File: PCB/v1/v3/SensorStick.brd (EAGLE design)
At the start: 76.2 x 44.5 mm, 74 parts, among them U1 TPD4F003DQDR, Y1 ECS-TXO-3225MV-400-TR

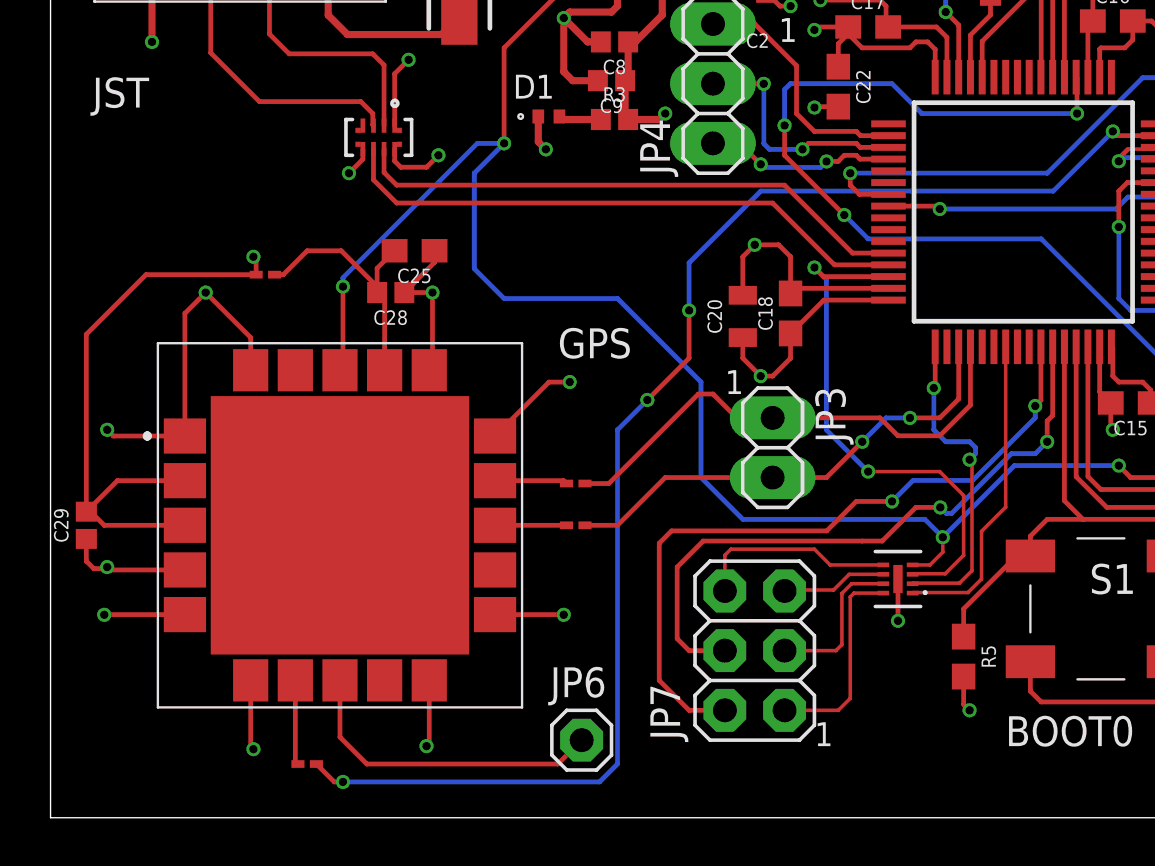
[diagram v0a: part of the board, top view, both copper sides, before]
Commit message: Jesus - Began to transition GPS to header pins
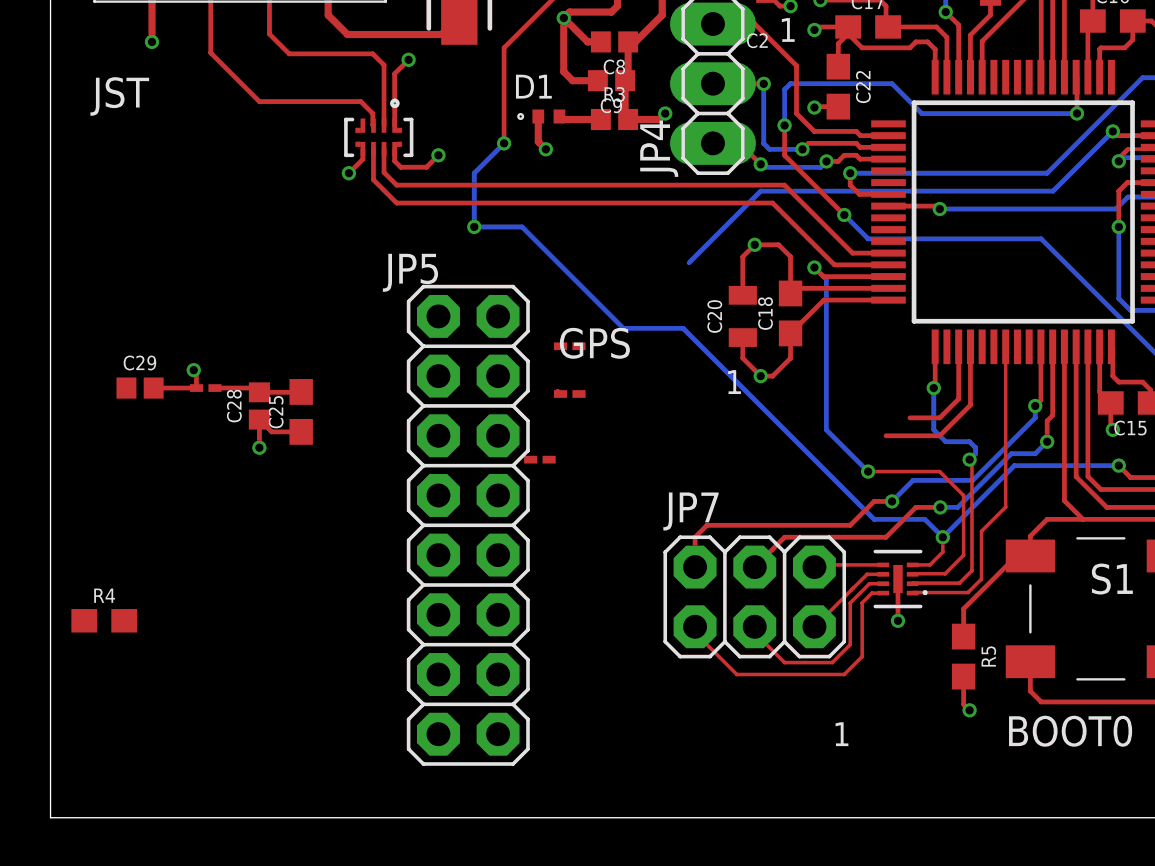
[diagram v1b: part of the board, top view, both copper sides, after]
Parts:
- removed GPS: SAM-M8Q-0-10, SAM-M8Q-0-10:SAMM8Q010
- removed JP3: (no value), pinhead:1X02
- removed JP6: (no value), pinhead:1X01
- added JP5: (no value), pinhead:2X08
- added R4: 0, SparkFun-Resistors:0603
- moved L4 16.3 mm to (20.8, 15.2)
- moved C25 8.39 mm to (10.7, 17.3), turned to 90 degrees
- moved L2 7.62 mm to (22.1, 20.1)
- moved C28 7.38 mm to (8.89, 17.5), turned to 90 degrees
- moved C29 6.27 mm to (3.81, 18.3), turned to 0 degrees
- moved L6 5.45 mm to (6.60, 18.3)
- moved L5 3.82 mm to (22.1, 18.0)
- moved JP7 2.29 mm to (30.0, 9.40), turned to 0 degrees
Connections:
- removed net N$2: GPS.7, L4.2
- removed net N$9: C25.2, C28.2, GPS.17, L6.1
- new net TIMEPULSE: JP5.6, L4.2
- new net VCC: JP5.1
- new net VCC_GPS: C25.2, C28.2, L6.1
- new net VCC_IO: JP5.7
- new net V_BACKUP: JP5.5
- net 3V3: now also R4.1, R4.2; no longer GPS.2, GPS.3
- net GND: now also JP5.10, JP5.11, JP5.12, JP5.13, JP5.14, JP5.15, JP5.16, JP5.9; no longer GPS.1, GPS.10, GPS.11, GPS.15, GPS.16, GPS.20, GPS.4, GPS.5, GPS.6
- net GPS_SAFEBOOT: now also JP5.8; no longer GPS.8, JP6.1
- net NRST: now also JP5.3; no longer GPS.18
- net RX: now also JP5.4; no longer GPS.14
- net TX: now also JP5.2; no longer GPS.13
- net USART3_RX: no longer JP3.1
- net USART3_TX: no longer JP3.2
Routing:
- net GND: track 180.0 -> 140.6 mm, vias 39 -> 31
- net GPIO_EXTI1: track 58.4 -> 22.4 mm, vias 4 -> 1
- net 3V3: track 146.6 -> 123.4 mm
- net NRST: track 115.0 -> 98.4 mm
- net USART3_TX: track 20.4 -> 4.63 mm, vias 2 -> 0
- net USART3_RX: track 21.7 -> 6.61 mm
- net GPS_SAFEBOOT: track 13.6 -> 0.00 mm
- net N$9: track 10.9 -> 0.00 mm
- net USART1_TX: track 30.5 -> 21.0 mm
- net USART1_RX: track 27.6 -> 18.8 mm
- net NRST_O: track 8.65 -> 2.97 mm
- net VCC_GPS: track 0.00 -> 4.31 mm
- net N$2: track 3.61 -> 0.00 mm
- net TX: track 3.04 -> 0.00 mm
- net SWO_O: track 8.80 -> 11.8 mm
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
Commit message: Jesus - Cleaning up GPS schematic
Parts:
- moved L4 1.27 mm to (21.8, 16.0)
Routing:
- net I2C3_SDA: track 37.3 -> 19.8 mm, vias 2 -> 1
- net I2C3_SCL: track 36.0 -> 20.8 mm, vias 2 -> 1
- net NRST: track 98.4 -> 94.5 mm, vias 4 -> 3
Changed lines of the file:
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@@
 <attribute name="NAME" x="23.9014" y="20.447" size="1.27" layer="27" ratio="6" rot="SR0"/>
 </element>
-<element name="L4" library="BLM03AG601SN1D" package="IND_BLM03_0201_MUR" value="BLM03AG601SN1D" x="20.828" y="15.24" smashed="yes" rot="R180">
-<attribute name="COPYRIGHT" value="Copyright (C) 2023 Ultra Librarian. All rights reserved." x="20.828" y="15.24" size="1.778" layer="27" rot="R180" display="off"/>
-<attribute name="DIGI-KEY_PART_NUMBER_1" value="490-5164-1-ND" x="20.828" y="15.24" size="1.778" layer="27" rot="R180" display="off"/>
-<attribute name="DIGI-KEY_PART_NUMBER_2" value="490-5164-2-ND" x="20.828" y="15.24" size="1.778" layer="27" rot="R180" display="off"/>
-<attribute name="DIGI-KEY_PART_NUMBER_3" value="490-5164-6-ND" x="20.828" y="15.24" size="1.778" layer="27" rot="R180" display="off"/>
-<attribute name="MANUFACTURER_PART_NUMBER" value="BLM03AG601SN1D" x="20.828" y="15.24" size="1.778" layer="27" rot="R180" display="off"/>
-<attribute name="MFR_NAME" value="Murata" x="20.828" y="15.24" size="1.778" layer="27" rot="R180" display="off"/>
-<attribute name="NAME" x="21.6154" y="13.843" size="1.27" layer="27" ratio="6" rot="SR0"/>
+<element name="L4" library="BLM03AG601SN1D" package="IND_BLM03_0201_MUR" value="BLM03AG601SN1D" x="21.844" y="16.002" smashed="yes" rot="R180">
+<attribute name="COPYRIGHT" value="Copyright (C) 2023 Ultra Librarian. All rights reserved." x="21.844" y="16.002" size="1.778" layer="27" rot="R180" display="off"/>
+<attribute name="DIGI-KEY_PART_NUMBER_1" value="490-5164-1-ND" x="21.844" y="16.002" size="1.778" layer="27" rot="R180" display="off"/>
+<attribute name="DIGI-KEY_PART_NUMBER_2" value="490-5164-2-ND" x="21.844" y="16.002" size="1.778" layer="27" rot="R180" display="off"/>
+<attribute name="DIGI-KEY_PART_NUMBER_3" value="490-5164-6-ND" x="21.844" y="16.002" size="1.778" layer="27" rot="R180" display="off"/>
+<attribute name="MANUFACTURER_PART_NUMBER" value="BLM03AG601SN1D" x="21.844" y="16.002" size="1.778" layer="27" rot="R180" display="off"/>
+<attribute name="MFR_NAME" value="Murata" x="21.844" y="16.002" size="1.778" layer="27" rot="R180" display="off"/>
+<attribute name="NAME" x="22.6314" y="14.605" size="1.27" layer="27" ratio="6" rot="SR0"/>
 </element>
 <element name="L5" library="BLM03AG601SN1D" package="IND_BLM03_0201_MUR" value="BLM03AG601SN1D" x="22.098" y="18.034" smashed="yes" rot="R180">
@@
 <wire x1="59.436" y1="16.764" x2="59.436" y2="20.408" width="0.2032" layer="1"/>
 <via x="59.69" y="16.51" extent="1-16" drill="0.35"/>
-<wire x1="59.69" y1="16.51" x2="59.69" y2="12.7" width="0.2032" layer="16"/>
-<wire x1="59.69" y1="12.7" x2="61.976" y2="10.414" width="0.2032" layer="16"/>
-<wire x1="61.976" y1="10.414" x2="61.976" y2="6.604" width="0.2032" layer="16"/>
 <contactref element="JP2" pad="4"/>
-<via x="61.976" y="6.604" extent="1-16" drill="0.35"/>
-<wire x1="61.976" y1="6.604" x2="62.738" y2="5.842" width="0.2032" layer="1"/>
-<wire x1="62.738" y1="5.842" x2="62.738" y2="2.54" width="0.2032" layer="1"/>
+<wire x1="62.738" y1="2.54" x2="61.677" y2="15.53" width="0" layer="19" extent="1-1"/>
 </signal>
 <signal name="I2C3_SDA">
@@
 <wire x1="56.73" y1="23.788" x2="54.991" y2="25.527" width="0.2032" layer="1"/>
 <via x="60.452" y="18.034" extent="1-16" drill="0.35"/>
-<wire x1="60.452" y1="18.034" x2="60.452" y2="13.462" width="0.2032" layer="16"/>
-<wire x1="62.738" y1="11.176" x2="62.738" y2="8.636" width="0.2032" layer="16"/>
-<wire x1="60.452" y1="13.462" x2="62.738" y2="11.176" width="0.2032" layer="16"/>
 <contactref element="JP2" pad="3"/>
-<via x="62.738" y="8.636" extent="1-16" drill="0.35"/>
-<wire x1="62.738" y1="8.636" x2="63.754" y2="7.62" width="0.2032" layer="1"/>
-<wire x1="63.754" y1="7.62" x2="63.754" y2="6.096" width="0.2032" layer="1"/>
-<wire x1="63.754" y1="6.096" x2="65.278" y2="4.572" width="0.2032" layer="1"/>
-<wire x1="65.278" y1="4.572" x2="65.278" y2="2.54" width="0.2032" layer="1"/>
 <wire x1="61.677" y1="18.03" x2="60.456" y2="18.03" width="0.2032" layer="1"/>
 <wire x1="60.456" y1="18.03" x2="60.452" y2="18.034" width="0.2032" layer="1"/>
+<wire x1="65.278" y1="2.54" x2="61.677" y2="18.03" width="0" layer="19" extent="1-1"/>
 </signal>
 <signal name="GPIO_EXTI2">
@@
 <wire x1="30.226" y1="26.67" x2="27.178" y2="23.622" width="0.2032" layer="16"/>
 <contactref element="L4" pad="1"/>
-<wire x1="21.2217" y1="15.24" x2="27.178" y2="23.622" width="0" layer="19" extent="1-16"/>
+<wire x1="22.2377" y1="16.002" x2="27.178" y2="23.622" width="0" layer="19" extent="1-16"/>
 </signal>
 <signal name="GPIO_EXTI3">
@@
 <wire x1="19.304" y1="32.76601875" x2="19.304" y2="28.702" width="0.2032" layer="1"/>
 <via x="19.304" y="28.702" extent="1-16" drill="0.35"/>
-<wire x1="37.2138" y1="12.7" x2="35.052" y2="12.7" width="0.2032" layer="16"/>
-<wire x1="26.924" y1="20.828" x2="24.384" y2="20.828" width="0.2032" layer="16"/>
-<wire x1="24.384" y1="20.828" x2="20.066" y2="25.146" width="0.2032" layer="16"/>
-<wire x1="18.034" y1="25.146" x2="20.066" y2="25.146" width="0.2032" layer="16"/>
-<wire x1="18.034" y1="25.146" x2="18.034" y2="27.432" width="0.2032" layer="16"/>
-<wire x1="18.034" y1="27.432" x2="19.304" y2="28.702" width="0.2032" layer="16"/>
-<wire x1="35.052" y1="12.7" x2="26.924" y2="20.828" width="0.2032" layer="16"/>
+<wire x1="37.2138" y1="12.7" x2="35.306" y2="12.7" width="0.2032" layer="16"/>
+<wire x1="35.306" y1="12.7" x2="19.304" y2="28.702" width="0.2032" layer="16"/>
 <contactref element="U1" pad="4"/>
 <wire x1="36.693" y1="10.76" x2="37.43" y2="10.76" width="0.1524" layer="1"/>
@@
 <wire x1="58.801" y1="13.589" x2="59.905" y2="13.589" width="0.2032" layer="1"/>
 <contactref element="JP5" pad="3"/>
-<via x="18.034" y="25.146" extent="1-16" drill="0.35"/>
-<wire x1="16.51" y1="18.796" x2="18.034" y2="25.146" width="0" layer="19" extent="1-1"/>
+<wire x1="16.51" y1="18.796" x2="19.304" y2="28.702" width="0" layer="19" extent="1-1"/>
 </signal>
 <signal name="DP">
@@
 <contactref element="JP5" pad="6"/>
 <contactref element="L4" pad="2"/>
-<wire x1="19.05" y1="16.256" x2="20.4343" y2="15.24" width="0" layer="19" extent="1-1"/>
+<wire x1="19.05" y1="16.256" x2="21.4503" y2="16.002" width="0" layer="19" extent="1-1"/>
 </signal>
 </signals>

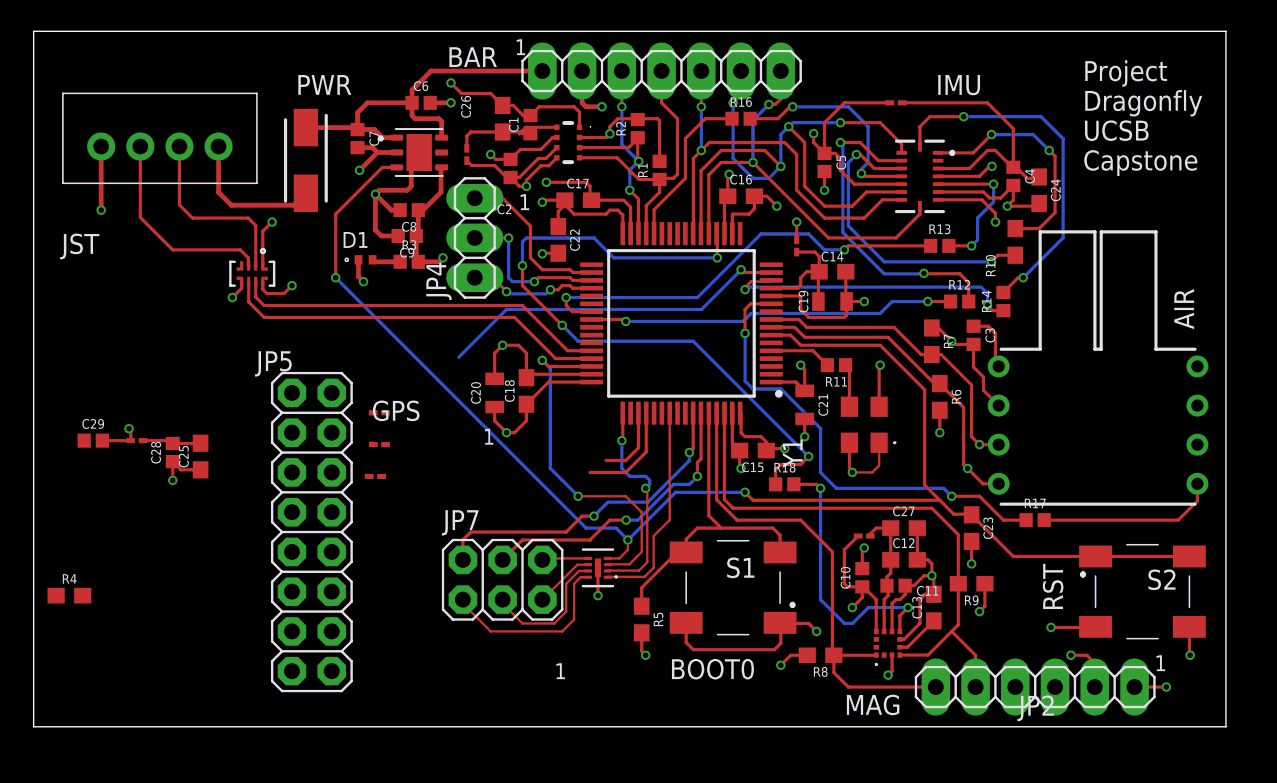
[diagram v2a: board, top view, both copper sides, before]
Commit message: Jesus - Further updates to Mag/GPS/USART breakout
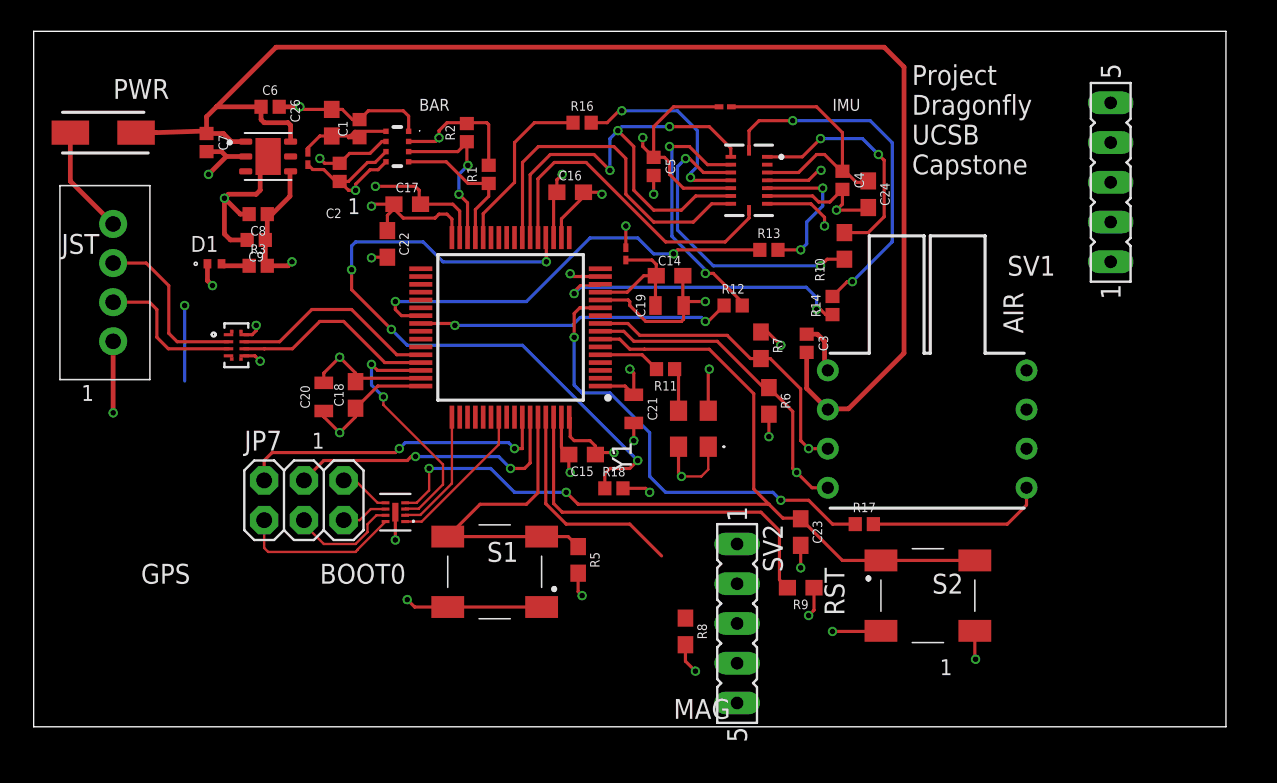
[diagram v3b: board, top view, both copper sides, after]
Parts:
- removed C10, C11, C28, C29: 0.1uF, SparkFun-Capacitors:0402
- removed C12: 10uF, SparkFun-Capacitors:0603
- removed C13: 0.22uF, SparkFun-Capacitors:0603
- removed C25, C27: 4.7uF, SparkFun-Capacitors:0603
- removed JP1: (no value), pinhead:1X07
- removed JP2: (no value), pinhead:1X06
- removed JP4: (no value), pinhead:1X03
- removed JP5: (no value), pinhead:2X08
- removed L2, L4, L5, L6, L8: BLM03AG601SN1D, BLM03AG601SN1D:IND_BLM03_0201_MUR
- removed MAGNETOMETER: IIS2MDCTR, IIS2MDCTR:IIS2MDCTR
- removed R4: 0, SparkFun-Resistors:0603
- added SV1, SV2: (no value), con-lsta:FE05-1
- moved S1 15.3 mm to (29.5, 9.91)
- moved R12 14.5 mm to (44.7, 26.9)
- moved S2 13.7 mm to (57.1, 8.38)
- moved JP7 13.7 mm to (17.3, 14.5)
- moved U1 13.4 mm to (23.1, 13.7)
- moved U$1 13.1 mm to (4.45, 38.0), turned to 180 degrees
- moved JST_CONNECTION 12.5 mm to (5.08, 24.6), turned to 90 degrees
- moved L1 10.9 mm to (37.8, 30.2)
- moved AIRSPEED 10.9 mm to (59.1, 23.9)
- moved C16 10.9 mm to (34.3, 34.2)
- moved C21 10.9 mm to (38.4, 20.3)
- moved C23 10.9 mm to (49.0, 12.4)
- moved IMU 10.9 mm to (45.7, 34.9)
- moved L3 10.9 mm to (44.2, 39.6)
- moved R1 10.9 mm to (29.1, 35.3)
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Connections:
- removed net GPS_SAFEBOOT: JP5.8
- removed net N$10: C11.1, C12.1, C27.1, L8.1, MAGNETOMETER.9
- removed net N$7: C13.1, MAGNETOMETER.5
- removed net RX: JP5.4, L5.2
- removed net SPI2_MISO: JP4.2, MICROCONTROLLER.35
- removed net SPI2_MOSI: JP4.1, MICROCONTROLLER.36
- removed net SPI2_SCK: JP4.3, MICROCONTROLLER.34
- removed net TIMEPULSE: JP5.6, L4.2
- removed net TX: JP5.2, L2.2
- removed net VCC: JP5.1
- removed net VCC_GPS: C25.2, C28.2, L6.1
- removed net VCC_IO: JP5.7
- removed net V_BACKUP: JP5.5
- new net USART2_RX: MICROCONTROLLER.17, SV1.3
- new net USART2_TX: MICROCONTROLLER.16, SV1.2
- net 3V3: now also SV1.5, SV2.5; no longer AIRSPEED.2, C10.1, C29.2, C3.2, JP2.1, L6.2, L8.2, MAGNETOMETER.10, MAGNETOMETER.3, R4.1, R4.2
- net 5V: now also AIRSPEED.2, C3.2; no longer JP1.1
- net EXTI4: now also SV2.1; no longer MAGNETOMETER.7
- net GND: now also SV1.4, SV2.4; no longer C10.2, C11.2, C12.2, C13.2, C25.1, C27.2, C28.1, C29.1, JP1.2, JP2.2, JP5.10, JP5.11, JP5.12, JP5.13, JP5.14, JP5.15, JP5.16, JP5.9, MAGNETOMETER.6, MAGNETOMETER.8
- net GPIO_EXTI1: now also SV1.1; no longer L4.1
- net I2C1_SCL: now also SV2.3; no longer JP2.6, MAGNETOMETER.1
- net I2C1_SDA: now also SV2.2; no longer JP2.5, MAGNETOMETER.4
- net I2C2_SCL: no longer JP1.4
- net I2C2_SDA: no longer JP1.3
- net I2C3_SCL: no longer JP2.4
- net I2C3_SDA: no longer JP2.3
- net NRST: no longer JP5.3
- net SPI1_MISO: no longer JP1.6
- net SPI1_MOSI: no longer JP1.5
- net SPI1_SCK: no longer JP1.7
- net USART3_RX: no longer L5.1
- net USART3_TX: no longer L2.1
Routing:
- net 5V: track 24.4 -> 90.9 mm
- net GND: track 140.6 -> 109.9 mm, vias 31 -> 25
- net NRST: track 94.5 -> 64.1 mm
- net 3V3: track 123.4 -> 95.0 mm, vias 21 -> 16
- net GPIO_EXTI1: track 22.4 -> 2.00 mm
- net I2C1_SCL: track 31.9 -> 14.3 mm
- net EXTI4: track 17.3 -> 1.81 mm, vias 2 -> 1
- net USB_DP: track 24.7 -> 13.1 mm
- net I2C1_SDA: track 35.9 -> 24.5 mm
- net SPI2_SCK: track 10.6 -> 0.00 mm
- net USB_DN: track 23.9 -> 13.3 mm
- net SPI2_MISO: track 10.3 -> 0.00 mm, vias 2 -> 0
- net SPI1_MISO: track 42.3 -> 32.6 mm, vias 4 -> 3
- net N$10: track 8.44 -> 0.00 mm
- net I2C2_SCL: track 17.8 -> 9.61 mm
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
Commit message: Jesus - Cleaned up sch/layout, finished
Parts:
- removed SV2: (no value), con-lsta:FE05-1
- added IC1: (no value), ic-package:DIL24-3
- added JP1: (no value), pinhead:2X03
- moved SV1 19.3 mm to (50.0, 30.2)
- moved C6 15.1 mm to (12.4, 24.8), turned to 270 degrees
- moved R9 14.3 mm to (34.8, 7.87)
- moved U$1 14.2 mm to (4.45, 23.7)
- moved JST_CONNECTION 14.0 mm to (5.08, 10.7)
- moved AIRSPEED 13.7 mm to (50.5, 13.1), turned to 180 degrees
- moved R17 13.7 mm to (39.6, 10.4), turned to 90 degrees
- moved S2 12.4 mm to (45.5, 4.32)
- moved R8 12.0 mm to (29.7, 7.11), turned to 0 degrees
- moved C23 11.8 mm to (39.4, 5.59)
- moved C7 10.8 mm to (13.8, 26.9), turned to 90 degrees
- moved R3 10.3 mm to (4.06, 29.3), turned to 270 degrees
- moved POWER_MODULE 9.89 mm to (10.2, 27.8), turned to 180 degrees
- moved R6 9.40 mm to (39.6, 15.0)
- moved C16 8.99 mm to (27.7, 28.1)
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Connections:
- net 3V3: now also JP1.1, JP1.3; no longer SV2.5
- net EXTI4: now also JP1.6; no longer SV2.1
- net GND: now also JP1.5; no longer SV2.4
- net I2C1_SCL: now also JP1.2; no longer SV2.3
- net I2C1_SDA: now also JP1.4; no longer SV2.2
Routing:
- net USART2_RX: track 0.00 -> 24.4 mm
- net USART2_TX: track 0.00 -> 23.0 mm
- net NRST: track 64.1 -> 86.1 mm, vias 3 -> 4
- net GPIO_EXTI1: track 2.00 -> 23.9 mm, vias 1 -> 0
- net I2C1_SDA: track 24.5 -> 15.8 mm
- net 3V3: track 95.0 -> 103.2 mm, vias 16 -> 19
- net EXTI3: track 11.4 -> 3.83 mm
- net EXTI4: track 1.81 -> 8.71 mm, vias 1 -> 2
- net GPIO_EXTI3: track 29.7 -> 23.5 mm
- net DN: track 11.2 -> 5.97 mm
- net USB_DP: track 13.1 -> 8.70 mm
- net USB_DN: track 13.3 -> 8.94 mm
- net GND: track 109.9 -> 114.2 mm, vias 25 -> 28
- net 5V: track 90.9 -> 94.9 mm
- net I2C3_SCL: track 20.8 -> 18.3 mm, vias 1 -> 0
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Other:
- board size 76.2 x 44.5 mm -> 58.4 x 38.1 mm
- board text added: "Jesus Oviedo Noah Lutz Teagan Connon Marko Ristic Danny Cardenas"
- board text added: "Project Dragonfly UCSB CE Capstone"
- board text added: "⠀⠀⠀⠀⠀⠀⢀⣀⣀⠀⠀⠀⠀⠀⠀⠀⠀⠀⠀⠀⠀⠀⠀⠀⠀⠀⠀⠀⠀⠀ ⠀⠀⠀⠀⠀⠀⣿⠉⠙⠻⣦⡀⠀⠀⠀⠀⠀⠀⠀⠀⠀⠀⠀⠀⠀⠀⠀⠀⠀⠀ ⠀⠀⢀⣶⠿⠶⣿⣄⠀⠀⠈⢿⣄⠀⠀⠀⠀⠀⠀⠀⠀⠀⠀⠀⠀⠀⠀⠀⠀⠀ ⠀⠀⠈⣧⠀⠀⠘⣿⣷⣄⠀⠀⢻⣦⠀⠀⣀⣄⡀⠀⠀⠀⠀⠀⠀⠀⠀⠀⠀⠀ ⠀⠀⠀⠘⣧⡀⠀⠘⣷⡙⢷⣄⠀⠹⣧⠀⢿⣿⣷⣦⡄⠀⠀⠀⠀⠀⠀⠀⠀⠀ ⠀⠀⠀⠀⠈⢿⣄⠀⠘⢷⡄⠹⣧⠀⠛⣂⠀⢸⣿⣿⣿⣄⠀⠀⠀⠀⠀⠀⠀⠀ ⠀⠀⠀⠀⠀⠀⠙⢷⣄⠈⠻⡦⠀⣠⣾⣿⣷⣤⠈⠙⠿⠿⠁⠀⠀⠀⠀⠀⠀⠀ ⠀⠀⠀⠀⠀⠀⠀⠀⠙⢷⣦⠀⣼⣿⣿⣿⣿⠟⠀⢶⣤⣄⡀⠀⠀⠀⠀⠀⠀⠀ ⠀⠀⠀⠀⠀⠀⠀⠀⠀⠀⠈⣀⣿⠿⠿⠛⢁⠰⣦⣀⠀⠉⠻⢶⣤⡀⠀⠀⠀⠀ ⠀⠀⠀⠀⠀⠀⠀⠀⢀⣤⣾⡟⠁⠠⣦⡀⠙⢷⣌⡛⢷⣄⠀⠀⠈⠻⢷⣄⠀⠀ ⠀⠀⠀⠀⠀⠀⣠⣶⣿⣿⠋⠀⠀⠀⠙⢷⣄⠀⠉⠻⢶⣽⣷⣄⠀⠀⠀⢻⣆⠀ ⠀⠀⠀⢀⣴⣾⣿⣿⠟⠁⠀⠀⠀⠀⠀⠀⠙⢷⣄⠀⠀⠈⠙⠻⣷⣶⣤⣴⠟⠀ ⠀⢠⣾⣿⣿⣿⡿⠋⠀⠀⠀⠀⠀⠀⠀⠀⠀⠀⠙⠻⣦⡀⠀⠀⠸⣧⠀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"
- board text removed: "Project Dragonfly UCSB Capstone"
